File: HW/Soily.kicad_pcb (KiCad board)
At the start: 2 copper layers, 25 x 129.5 mm, 52 parts, among them J1 USB4105-GF-A, SW1 Reset, U1 ESP32-H2-MINI-1, U2 USBLC6-2SC6, U3 AP2112K-3.3, U4 SHT30-DIS, U5 625L3C040M00000, U6 FDC2212DNTR, Y1 ABS07-32.768KHZ-T

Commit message: Missing testpad connections
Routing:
- net +3.3V: track 76.8 -> 79.3 mm, vias 5 -> 6
- net /BOOTMODE: track 3.61 -> 5.00 mm, vias 0 -> 1
- net GND: vias 76 -> 79
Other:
- board text added: "Soil moisture sensor v0.1 2025"
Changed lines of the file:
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@@
 			(crossoutdnponfab yes)
 			(subtractmaskfromsilk no)
-			(outputformat 1)
+			(outputformat 5)
 			(mirror no)
-			(drillshape 1)
+			(drillshape 0)
 			(scaleselection 1)
-			(outputdirectory "")
+			(outputdirectory "/Users/dan/Downloads/out/")
 		)
 	)
@@
 		)
 	)
+	(gr_text "Soil moisture sensor\nv0.1\n2025\n"
+		(at 95.92 40.64 0)
+		(layer "B.SilkS")
+		(effects
+			(font
+				(size 0.813 0.813)
+				(thickness 0.127)
+			)
+			(justify left bottom mirror)
+		)
+	)
 	(dimension
 		(type orthogonal)
@@
 	)
 	(segment
-		(start 94.026 55.5)
-		(end 94.05 55.524)
-		(width 0.3)
-		(layer "F.Cu")
-		(net 2)
-	)
-	(segment
 		(start 85.4 54.2)
 		(end 85.4 54.5)
@@
 	)
 	(via
+		(at 85.4 61.9)
+		(size 0.508)
+		(drill 0.254)
+		(layers "F.Cu" "B.Cu")
+		(free yes)
+		(net 2)
+	)
+	(via
 		(at 84.95 46.75)
 		(size 0.508)
@@
 	)
 	(via
+		(at 89.5 57.2)
+		(size 0.508)
+		(drill 0.254)
+		(layers "F.Cu" "B.Cu")
+		(free yes)
+		(net 2)
+	)
+	(via
+		(at 87 57.2)
+		(size 0.508)
+		(drill 0.254)
+		(layers "F.Cu" "B.Cu")
+		(free yes)
+		(net 2)
+	)
+	(via
 		(at 83.95 45.75)
 		(size 0.508)
@@
 	(segment
 		(start 85.4 57.825)
-		(end 85.4 57.5)
+		(end 85.4 56.05)
+		(width 0.4)
+		(layer "F.Cu")
+		(net 5)
+	)
+	(segment
+		(start 77.6 74.5)
+		(end 78.35 75.25)
 		(width 0.4)
 		(layer "F.Cu")
@@
 	)
 	(segment
+		(start 77.7 75.9)
+		(end 78.35 75.25)
+		(width 0.2)
+		(layer "F.Cu")
+		(net 5)
+	)
+	(segment
 		(start 78.6 68.5)
 		(end 79.25 68.5)
@@
 	)
 	(segment
-		(start 85.4 57.5)
-		(end 85.4 56.05)
-		(width 0.4)
-		(layer "F.Cu")
-		(net 5)
-	)
-	(segment
 		(start 77.6 69.5)
 		(end 77.6 63.725)
@@
 	)
 	(segment
-		(start 77.6 74.5)
+		(start 78.35 75.25)
 		(end 78.95 75.85)
 		(width 0.4)
@@
 	)
 	(via
+		(at 77.7 75.9)
+		(size 0.508)
+		(drill 0.254)
+		(layers "F.Cu" "B.Cu")
+		(net 5)
+	)
+	(via
 		(at 78.9 44.35)
 		(size 0.508)
@@
 	)
 	(segment
+		(start 77.7 77.5)
+		(end 77.7 75.9)
+		(width 0.2)
+		(layer "B.Cu")
+		(net 5)
+	)
+	(segment
 		(start 79.35 44.35)
 		(end 79.95 44.95)
@@
 	(segment
 		(start 87.95 51.95)
-		(end 89.9 53.9)
+		(end 89.48 53.48)
 		(width 0.2)
 		(layer "F.Cu")
@@
 	)
 	(segment
+		(start 89.48 53.48)
+		(end 89.9 53.9)
+		(width 0.2)
+		(layer "F.Cu")
+		(net 15)
+	)
+	(via
+		(at 89.48 53.48)
+		(size 0.508)
+		(drill 0.254)
+		(layers "F.Cu" "B.Cu")
+		(net 15)
+	)
+	(segment
+		(start 89.48 53.48)
+		(end 88.48 53.48)
+		(width 0.2)
+		(layer "B.Cu")
+		(net 15)
+	)
+	(segment
+		(start 88.48 53.48)
+		(end 88.2 53.2)
+		(width 0.2)
+		(layer "B.Cu")
+		(net 15)
+	)
+	(segment
 		(start 77.525 56.025)
 		(end 78.3 55.25)
@@
 	(segment
 		(start 91.05 45.15)
-		(end 91.35 45.45)
+		(end 91.5 45.6)
 		(width 0.2)
 		(layer "F.Cu")
@@
 	)
 	(segment
-		(start 91.5 45.6)
-		(end 91.35 45.45)
-		(width 0.2)
-		(layer "F.Cu")
-		(net 19)
-	)
-	(segment
 		(start 77.1 48.625)
 		(end 76.825 48.35)
@@
 	)
 	(segment
-		(start 88.75 51.349)
-		(end 88.75 51.65)
-		(width 0.2)
-		(layer "F.Cu")
-		(net 45)
-	)
-	(segment
 		(start 79.3477 74.3)
 		(end 80 74.3)
@@
 	)
 	(zone
-		(net 0)
-		(net_name "")
-		(layers "F.Cu" "B.Cu")
-		(name "Ant Left")
-		(hatch edge 0.5)
-		(connect_pads
-			(clearance 0)
-		)
-		(min_thickness 0.25)
-		(filled_areas_thickness no)
-		(keepout
-			(tracks allowed)
-			(vias allowed)
-			(pads allowed)
-			(copperpour not_allowed)
-			(footprints allowed)
-		)
-		(placement
-			(enabled no)
-			(sheetname "/")
-		)
-		(fill
-			(thermal_gap 0.5)
-			(thermal_bridge_width 0.5)
-		)
-		(polygon
-			(pts
-				(xy 75 41.2) (xy 77.3 41.2) (xy 77.3 41.3) (xy 75 42.6)
-			)
-		)
-	)
-	(zone

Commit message: Cleanup component selection
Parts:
- D4: value XL-5050RGBC -> 150505M173300; footprint LED_SMD:LED_RGB_5050-6 -> ul_150505M173300:LED_150505M173300_WRE
- L1: footprint Inductor_SMD:L_0603_1608Metric -> Inductor_SMD:L_1210_3225Metric
- U4: value SHT30-DIS -> SHT40; footprint Sensor_Humidity:Sensirion_DFN-8-1EP_2.5x2.5mm_P0.5mm_EP1.1x1.7mm -> Sensor_Humidity:Sensirion_DFN-4_1.5x1.5mm_P0.8mm_SHT4x_NoCentralPad
- U6: value FDC2212DNTR -> FDC2212
- moved L1 0.90 mm to (87.4, 80.1)
- moved R10 0.10 mm to (98.4, 48.3)
- moved R12 0.10 mm to (95.2, 48.3)
- moved R11 0.10 mm to (96.8, 48.3)
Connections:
- U4 pad 2: GND -> /SCL
- U4 pad 3: unconnected-(U4-ALERT-Pad3) -> +3.3V
- U4 pad 4: /SCL -> GND
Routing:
- net GND: track 23.5 -> 18.5 mm, vias 79 -> 92
- net /SDA: track 31.9 -> 32.5 mm
- net /SCL: track 30.6 -> 31.2 mm
- net /SENSE_SOIL-: track 44.8 -> 45.3 mm
- net /SENSE_SOIL+: track 44.8 -> 45.3 mm
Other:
- board text added: "SHT40"
- board text removed: "SHT30"

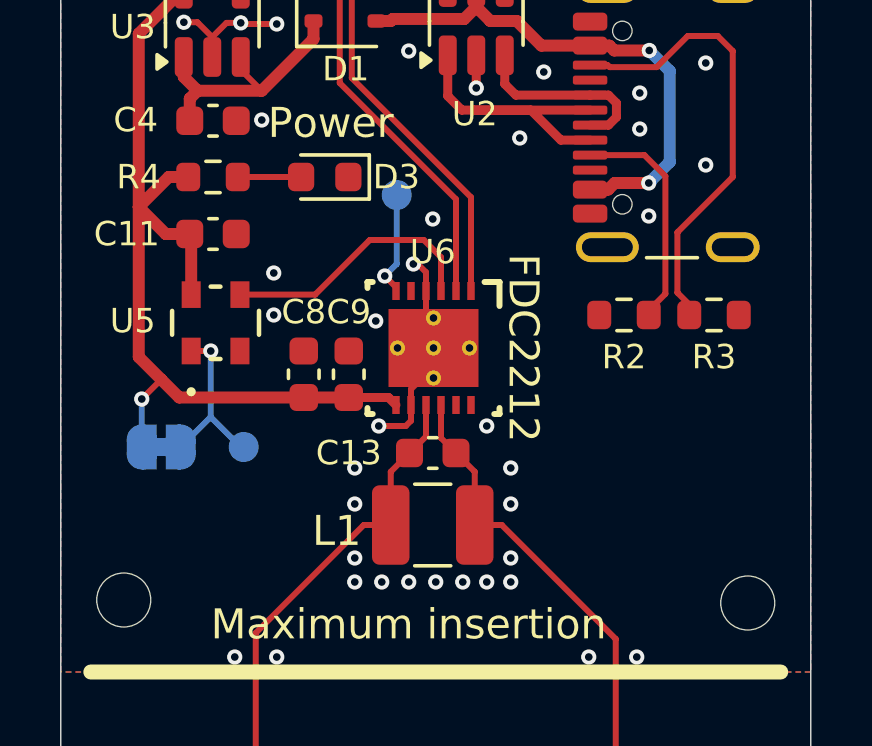
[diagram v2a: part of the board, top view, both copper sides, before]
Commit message: FDC2212 Breakout board
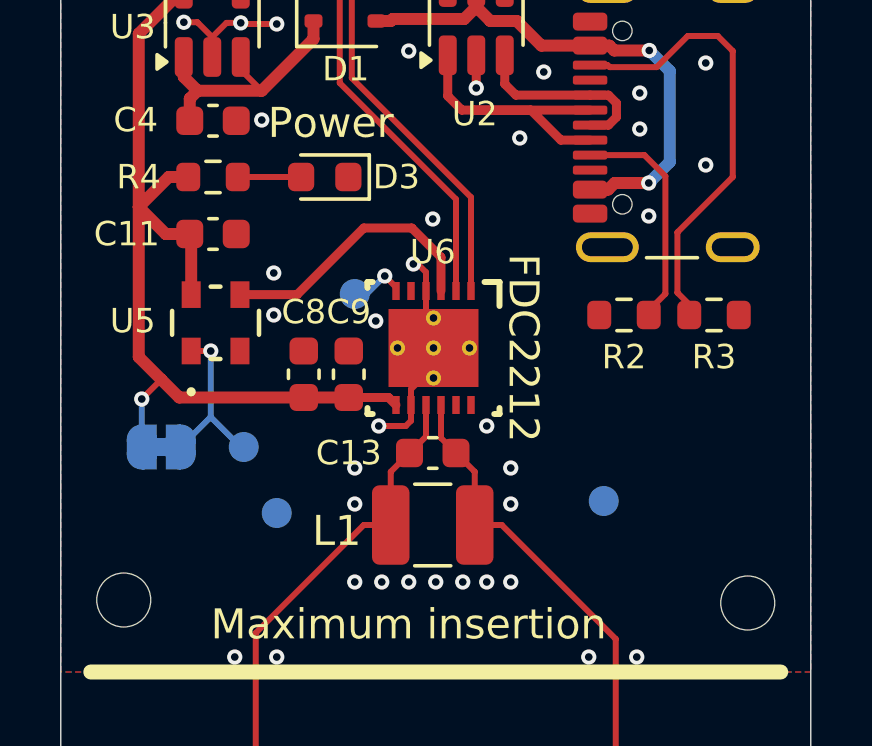
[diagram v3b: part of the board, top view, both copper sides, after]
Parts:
- added TP12: SOIL_B, TestPoint:TestPoint_Pad_D1.0mm, B.Cu at (93.1, 79.3)
- added TP9: SOIL_A, TestPoint:TestPoint_Pad_D1.0mm, B.Cu at (82.2, 79.7)
- moved TP11 3.58 mm to (84.8, 72.4)
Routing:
- net /FDC_OFF: track 3.52 -> 1.90 mm
- net GND: vias 92 -> 90
